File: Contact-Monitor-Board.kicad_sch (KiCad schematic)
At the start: 81 parts, among them J1 Screw_Terminal_01x02, J10 Screw_Terminal_01x02, J11 Screw_Terminal_01x02, J12 Screw_Terminal_01x02, J13 Screw_Terminal_01x02, J14 Screw_Terminal_01x02, J15 Screw_Terminal_01x02, J16 Screw_Terminal_01x02, J2 Screw_Terminal_01x02, J3 Screw_Terminal_01x02, J4 Screw_Terminal_01x02, J5 Screw_Terminal_01x02, J6 Screw_Terminal_01x02, J7 Screw_Terminal_01x02, J8 Screw_Terminal_01x02, J9 Screw_Terminal_01x02, Q1 2N7002, Q10 2N7002, Q11 2N7002, Q12 2N7002, Q13 2N7002, Q14 2N7002, Q15 2N7002, Q16 2N7002, Q2 2N7002, Q3 2N7002, Q4 2N7002, Q5 2N7002, Q6 2N7002, Q7 2N7002, Q8 2N7002, Q9 2N7002, SW1 SW_Nidec_CAS-120A1, U1 74HC4017D, U2 TLC555CD, U3 TPS61222DCK

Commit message: 接点電流と表示輝度を改善し、スキャンを9ステップ化
LED 電流制限抵抗を 1 kΩ → 470 Ω に変更。接点電流をピーク約 2.7 mA →
約 5.2 mA に引き上げ、接点酸化皮膜に対するマージンと LED の視認性を改善した。

- R18 を 1 kΩ → 4.7 kΩ に変更し、抵抗を 470 Ω / 4.7 kΩ の 2 種類に集約
- R20（4017 CLK プルアップ）を未実装化。TLC555 の出力が CMOS プッシュプル
  のため不要で、平均 0.48 mA の無駄な消費を削減
- 4017 の Q9 を MR に接続して自己リセットさせ、スキャンを 10 → 9 ステップに
  短縮。リフレッシュ 102 Hz → 113 Hz、デューティ 1/10 → 1/9
- README に「接続間違い時の動作」を追記。LED アノードを 4017 出力に接続して
  いる設計意図（VCC 直結にすると挿し間違いが誤点灯する）を明文化

Co-Authored-By: Claude Opus 5 <noreply@anthropic.com>
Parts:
- R1, R10, R11, R12, R13, R14, R15, R16, R17, R2, R3, R4, R5, R6, R7, R8, R9: value 1.0k -> 470
- R18: value 1.0k -> 4.7k
- R20: now not fitted; now left out of the parts list
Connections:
- net GND: no longer U1.15 (Reset)
- net at U1.11 (Q9): now also U1.15 (Reset)
- no-connect marks 3 -> 2

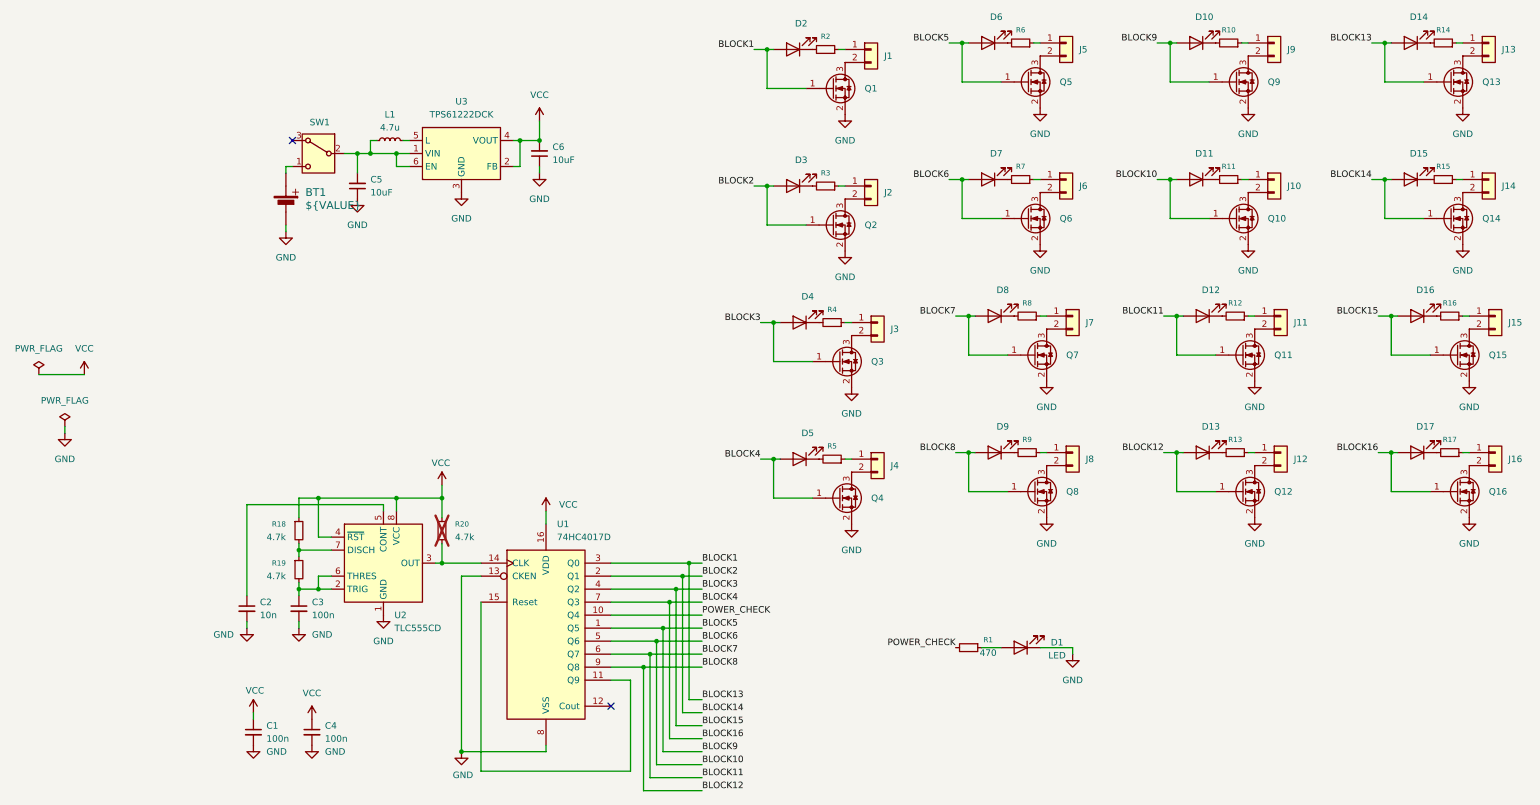
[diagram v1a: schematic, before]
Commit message: V1.3 公開に向けて設計データとドキュメントを整備
シルク:
- 警告文から Markdown 記法 [!WARNING] を除去し WARNING: に変更
- 裏面シルク回路図のリファレンス範囲を修正
  (D2-D14 -> D2-D17 / R2-R14 -> R2-R17 / J1-J13 -> J1-J16 / Q1-Q13 -> Q1-Q16)

基板・回路図:
- 観測用ヘッダ J17 (GND / +5V / CLK / RST、DNP) を追加
- 電源部のリレイアウトと、残っていた dangling via の除去 (DRC 0 件)
- PWR_FLAG を電池側へ移して ERC エラーを解消し、
  SW1 のフットプリント差分と U3 の L ピンを除外設定に登録
- 回路図タイトルブロックの日付を更新

製造データ:
- BOM/CPL の部品名を実発注品に合わせて修正
  (Screw_Terminal_01x02 -> JST VH 02 / SW_Nidec_CAS-120A1 -> KH-SS12D01-G3-5.0 /
   VALUE -> BH-AAA-A1AJ001)
- ガーバー・BOM・CPL・回路図 PDF を再生成

README:
- 電池の極性に関する警告を追加 (逆接保護回路なし)
- 観測用ヘッダ J17 の説明を追加

Co-Authored-By: Claude Opus 5 <noreply@anthropic.com>
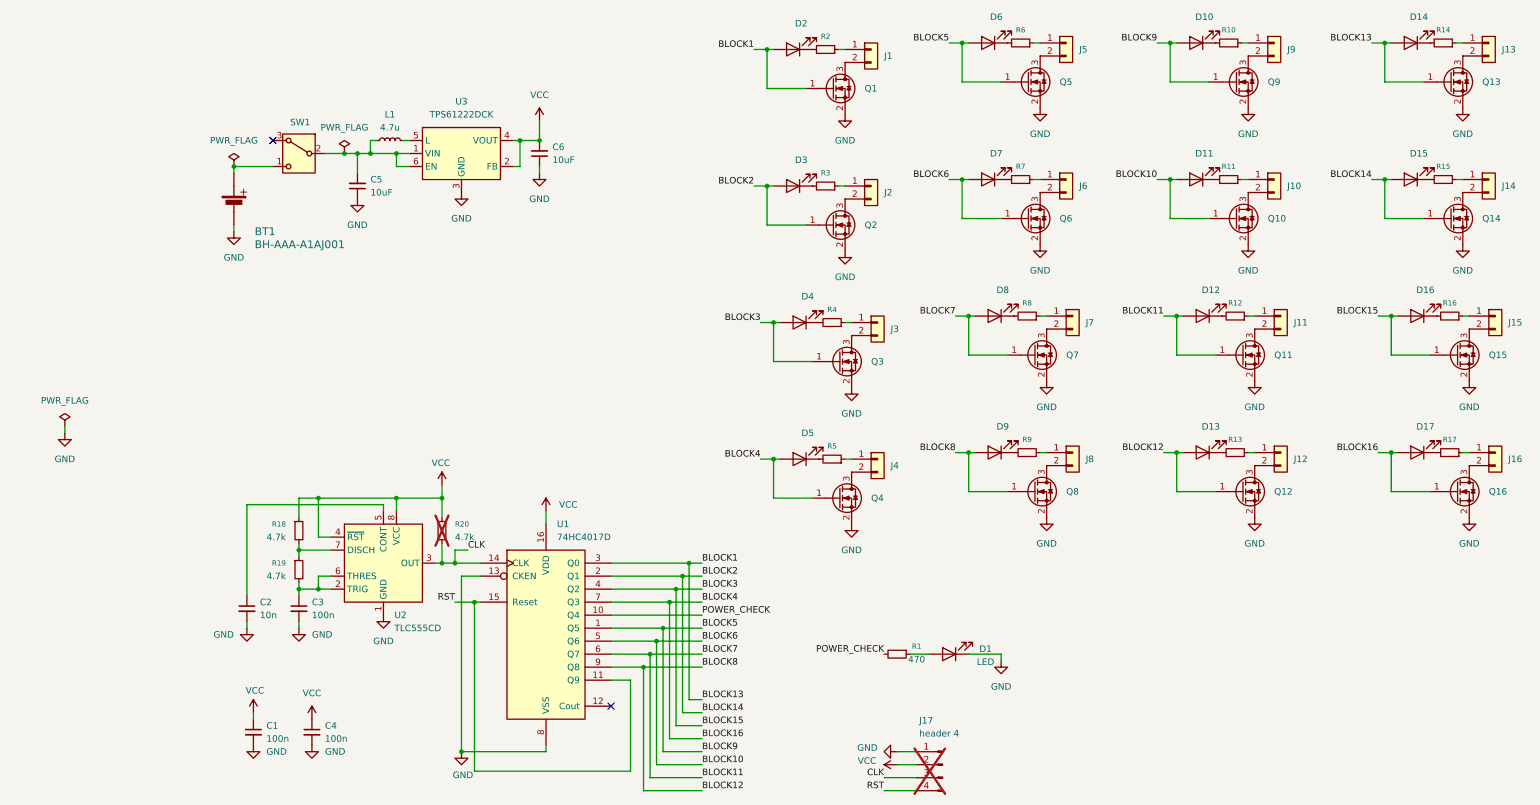
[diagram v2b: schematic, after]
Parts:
- added J17: header 4, Connector_PinHeader_2.54mm:PinHeader_1x04_P2.54mm_Vertical, symbol Connector:Conn_01x04_Pin
- BT1: value ${VALUE} -> BH-AAA-A1AJ001
- J1, J10, J11, J12, J13, J14, J15, J16, J2, J3, J4, J5, J6, J7, J8, J9: value Screw_Terminal_01x02 -> JST VH 02
- SW1: value SW_Nidec_CAS-120A1 -> KH-SS12D01-G3-5.0
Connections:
- net GND: now also J17.1 (Pin_1)
- net VCC: now also J17.2 (Pin_2)
- net RST: now reaches U1.11 (Q9), U1.15 (Reset)
- net RST: now also J17.4 (Pin_4)
- net CLK: now reaches R20.2, U1.14 (CLK), U2.3 (OUT)
- net CLK: now also J17.3 (Pin_3)
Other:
- moved on the sheet: BT1, D1, R1, SW1
